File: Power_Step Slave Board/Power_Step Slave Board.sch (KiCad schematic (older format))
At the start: 13 parts

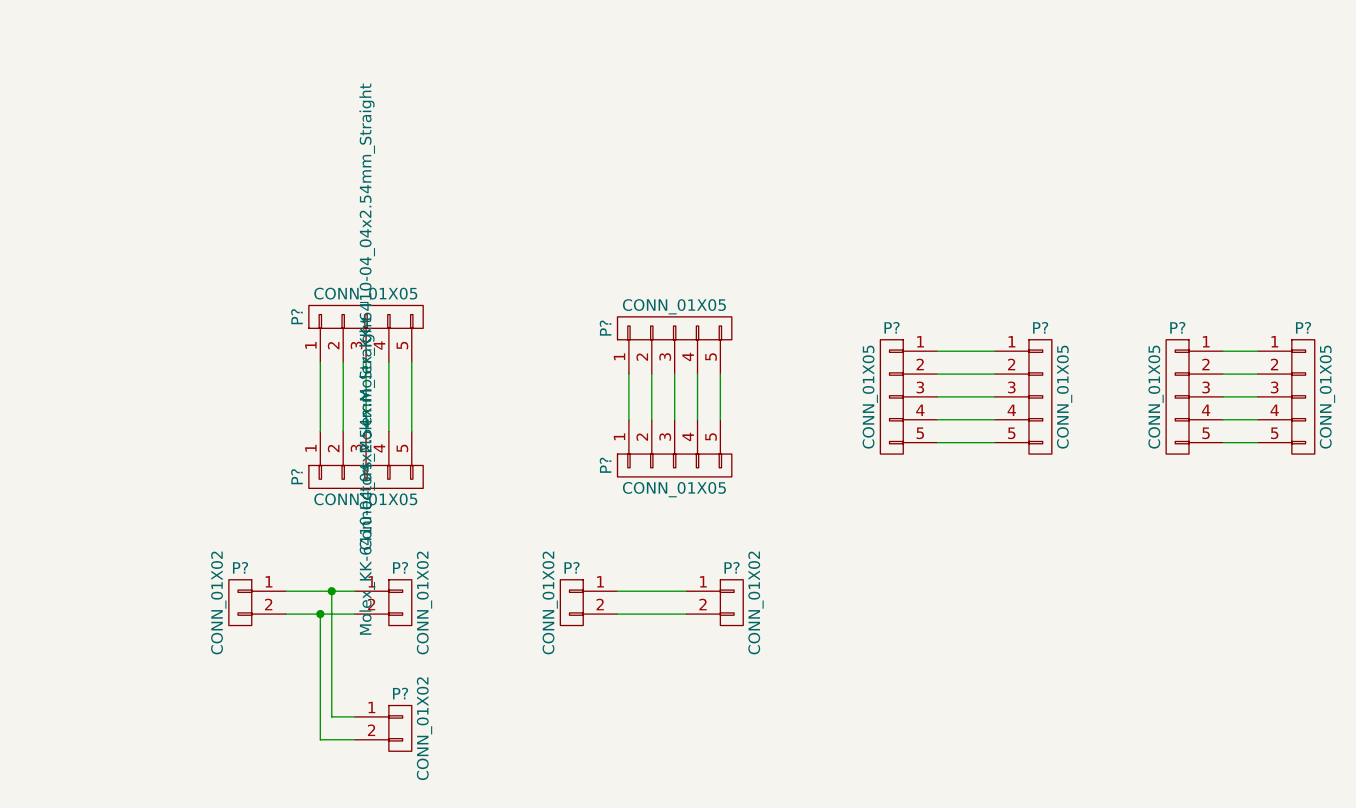
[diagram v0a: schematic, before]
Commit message: Updated connectors
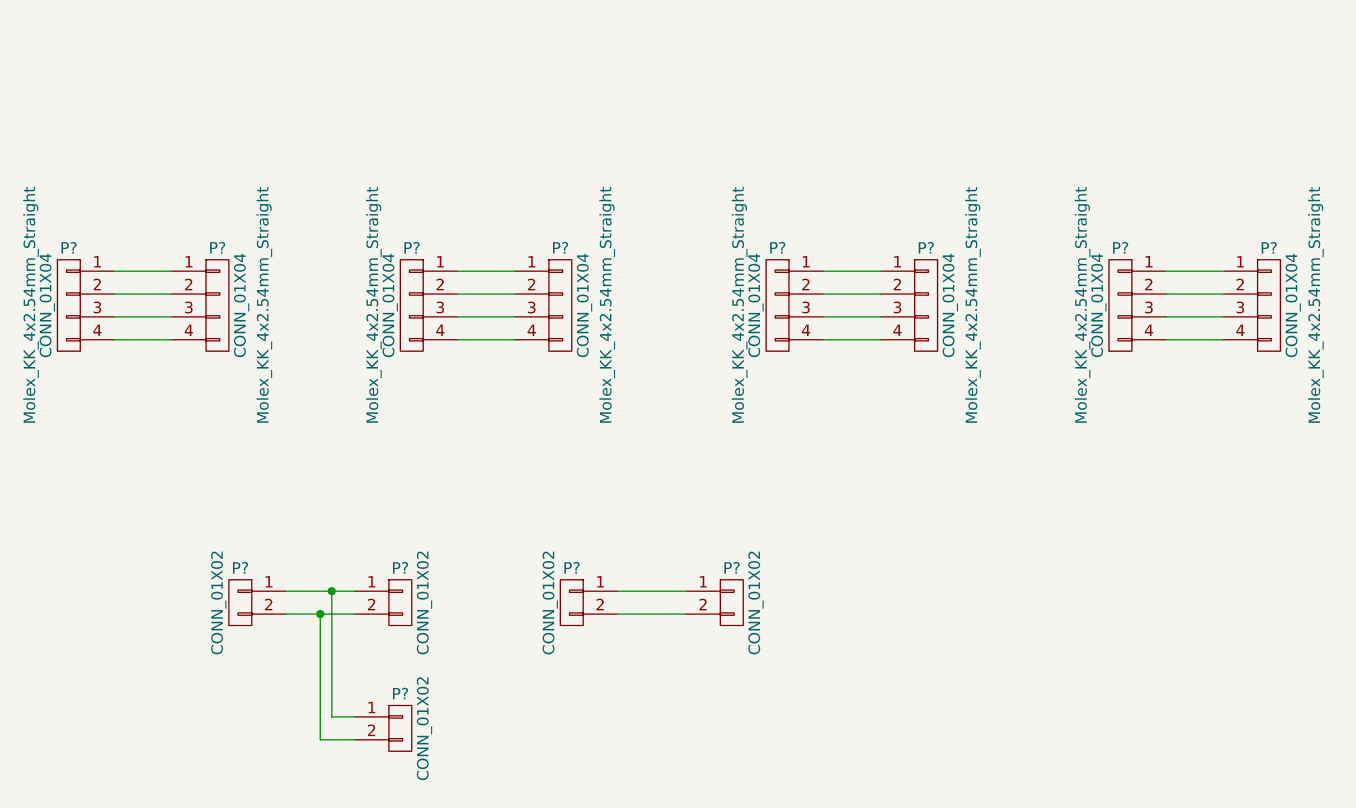
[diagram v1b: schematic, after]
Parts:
- removed P?: CONN_01X05, Molex_KK-6410-04_04x2.54mm_Straight, symbol CONN_01X05
- removed P?: CONN_01X05, Connectors_Molex:Molex_KK-6410-04_04x2.54mm_Straight, symbol CONN_01X05
- removed P? (x6): CONN_01X05, symbol CONN_01X05
- added P? (x8): CONN_01X04, Molex_KK_4x2.54mm_Straight, symbol CONN_01X04
- P?: footprint (none) -> ~
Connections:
- new net: P?.1 (P1), P?.1 (P1) (x4)
- new net: P?.2 (P2), P?.2 (P2) (x4)
- new net: P?.3 (P3), P?.3 (P3) (x4)
- new net: P?.4 (P4), P?.4 (P4) (x4)
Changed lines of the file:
@@
 $EndDescr
-$Comp
-L CONN_01X05 P?
-U 1 1 59DDF6DF
-P 2550 2200
-F 0 "P?" H 2550 2500 50  0000 C CNN
-F 1 "CONN_01X05" V 2650 2200 50  0000 C CNN
-F 2 "Molex_KK-6410-04_04x2.54mm_Straight" H 2550 2200 50  0000 C CNN
-F 3 "" H 2550 2200 50  0000 C CNN
-	1    2550 2200
-	0    -1   1    0
-$EndComp
-$Comp
-L CONN_01X05 P?
-U 1 1 59DDF732
-P 2550 1500
-F 0 "P?" H 2550 1800 50  0000 C CNN
-F 1 "CONN_01X05" V 2650 1500 50  0000 C CNN
-F 2 "Connectors_Molex:Molex_KK-6410-04_04x2.54mm_Straight" H 2550 1500 50  0000 C CNN
-F 3 "" H 2550 1500 50  0000 C CNN
-	1    2550 1500
-	0    -1   -1   0
-$EndComp
-$Comp
-L CONN_01X05 P?
-U 1 1 59DDF785
-P 3900 2150
-F 0 "P?" H 3900 2450 50  0000 C CNN
-F 1 "CONN_01X05" V 4000 2150 50  0000 C CNN
-F 2 "" H 3900 2150 50  0000 C CNN
-F 3 "" H 3900 2150 50  0000 C CNN
-	1    3900 2150
-	0    -1   1    0
-$EndComp
-$Comp
-L CONN_01X05 P?
-U 1 1 59DDF7DA
-P 3900 1550
-F 0 "P?" H 3900 1850 50  0000 C CNN
-F 1 "CONN_01X05" V 4000 1550 50  0000 C CNN
-F 2 "" H 3900 1550 50  0000 C CNN
-F 3 "" H 3900 1550 50  0000 C CNN
-	1    3900 1550
-	0    -1   -1   0
-$EndComp
-$Comp
-L CONN_01X05 P?
-U 1 1 59DDF859
-P 4850 1850
-F 0 "P?" H 4850 2150 50  0000 C CNN
-F 1 "CONN_01X05" V 4950 1850 50  0000 C CNN
-F 2 "" H 4850 1850 50  0000 C CNN
-F 3 "" H 4850 1850 50  0000 C CNN
-	1    4850 1850
-	-1   0    0    -1
-$EndComp
-$Comp
-L CONN_01X05 P?
-U 1 1 59DDF884
-P 5500 1850
-F 0 "P?" H 5500 2150 50  0000 C CNN
-F 1 "CONN_01X05" V 5600 1850 50  0000 C CNN
-F 2 "" H 5500 1850 50  0000 C CNN
-F 3 "" H 5500 1850 50  0000 C CNN
-	1    5500 1850
-	1    0    0    -1
-$EndComp
-$Comp
-L CONN_01X05 P?
-U 1 1 59DDF90B
-P 6100 1850
-F 0 "P?" H 6100 2150 50  0000 C CNN
-F 1 "CONN_01X05" V 6200 1850 50  0000 C CNN
-F 2 "" H 6100 1850 50  0000 C CNN
-F 3 "" H 6100 1850 50  0000 C CNN
-	1    6100 1850
-	-1   0    0    -1
-$EndComp
-$Comp
-L CONN_01X05 P?
-U 1 1 59DDF964
-P 6650 1850
-F 0 "P?" H 6650 2150 50  0000 C CNN
-F 1 "CONN_01X05" V 6750 1850 50  0000 C CNN
-F 2 "" H 6650 1850 50  0000 C CNN
-F 3 "" H 6650 1850 50  0000 C CNN
-	1    6650 1850
-	1    0    0    -1
-$EndComp
-Wire Wire Line
-	2350 2000 2350 1700
-Wire Wire Line
-	2450 1700 2450 2000
-Wire Wire Line
-	2550 2000 2550 1700
-Wire Wire Line
-	2650 1700 2650 2000
-Wire Wire Line
-	2750 2000 2750 1700
-Wire Wire Line
-	3700 1950 3700 1750
-Wire Wire Line
-	3800 1750 3800 1950
-Wire Wire Line
-	3900 1950 3900 1750
-Wire Wire Line
-	4000 1750 4000 1950
-Wire Wire Line
-	4100 1950 4100 1750
-Wire Wire Line
-	5050 2050 5300 2050
-Wire Wire Line
-	5300 1950 5050 1950
-Wire Wire Line
-	5050 1850 5300 1850
-Wire Wire Line
-	5300 1750 5050 1750
-Wire Wire Line
-	5050 1650 5300 1650
-Wire Wire Line
-	6300 1650 6450 1650
-Wire Wire Line
-	6450 1750 6300 1750
-Wire Wire Line
-	6300 1850 6450 1850
-Wire Wire Line
-	6450 1950 6300 1950
-Wire Wire Line
-	6300 2050 6450 2050
 $Comp
 L CONN_01X02 P?
@@
 F 0 "P?" H 2000 2900 50  0000 C CNN
 F 1 "CONN_01X02" V 2100 2750 50  0000 C CNN
-F 2 "" H 2000 2750 50  0000 C CNN
+F 2 "~" H 2000 2750 50  0000 C CNN
 F 3 "" H 2000 2750 50  0000 C CNN
 	1    2000 2750
@@
 Wire Wire Line
 	3950 2800 3650 2800
+$Comp
+L CONN_01X04 P?
+U 1 1 59E07C82
+P 1250 1450
+F 0 "P?" H 1250 1700 50  0000 C CNN
+F 1 "CONN_01X04" V 1350 1450 50  0000 C CNN
+F 2 "Molex_KK_4x2.54mm_Straight" V 1450 1450 50  0000 C BNN
+F 3 "" H 1250 1450 50  0000 C CNN
+	1    1250 1450
+	-1   0    0    -1
+$EndComp
+$Comp
+L CONN_01X04 P?
+U 1 1 59E07D10
+P 1900 1450
+F 0 "P?" H 1900 1700 50  0000 C CNN
+F 1 "CONN_01X04" V 2000 1450 50  0000 C CNN
+F 2 "Molex_KK_4x2.54mm_Straight" V 2100 1450 50  0000 C CNN
+F 3 "" H 1900 1450 50  0000 C CNN
+	1    1900 1450
+	1    0    0    -1
+$EndComp
+Wire Wire Line
+	1450 1300 1700 1300
+Wire Wire Line
+	1700 1400 1450 1400
+Wire Wire Line
+	1450 1500 1700 1500
+Wire Wire Line
+	1700 1600 1450 1600
+$Comp
+L CONN_01X04 P?
+U 1 1 59E081DD
+P 2750 1450
+F 0 "P?" H 2750 1700 50  0000 C CNN
+F 1 "CONN_01X04" V 2850 1450 50  0000 C CNN
+F 2 "Molex_KK_4x2.54mm_Straight" V 2950 1450 50  0000 C BNN
+F 3 "" H 2750 1450 50  0000 C CNN
+	1    2750 1450
+	-1   0    0    -1
+$EndComp
+$Comp
+L CONN_01X04 P?
+U 1 1 59E081E3
+P 3400 1450
+F 0 "P?" H 3400 1700 50  0000 C CNN
+F 1 "CONN_01X04" V 3500 1450 50  0000 C CNN
+F 2 "Molex_KK_4x2.54mm_Straight" V 3600 1450 50  0000 C CNN
+F 3 "" H 3400 1450 50  0000 C CNN
+	1    3400 1450
+	1    0    0    -1
+$EndComp
+Wire Wire Line
+	2950 1300 3200 1300
+Wire Wire Line
+	3200 1400 2950 1400
+Wire Wire Line
+	2950 1500 3200 1500
+Wire Wire Line
+	3200 1600 2950 1600
+$Comp
+L CONN_01X04 P?
+U 1 1 59E08812
+P 4350 1450
+F 0 "P?" H 4350 1700 50  0000 C CNN
+F 1 "CONN_01X04" V 4450 1450 50  0000 C CNN
+F 2 "Molex_KK_4x2.54mm_Straight" V 4550 1450 50  0000 C BNN
+F 3 "" H 4350 1450 50  0000 C CNN
+	1    4350 1450
+	-1   0    0    -1
+$EndComp
+$Comp
+L CONN_01X04 P?
+U 1 1 59E08818
+P 5000 1450
+F 0 "P?" H 5000 1700 50  0000 C CNN
+F 1 "CONN_01X04" V 5100 1450 50  0000 C CNN
+F 2 "Molex_KK_4x2.54mm_Straight" V 5200 1450 50  0000 C CNN
+F 3 "" H 5000 1450 50  0000 C CNN
+	1    5000 1450
+	1    0    0    -1
+$EndComp
+Wire Wire Line
+	4550 1300 4800 1300
+Wire Wire Line
+	4800 1400 4550 1400
+Wire Wire Line
+	4550 1500 4800 1500
+Wire Wire Line
+	4800 1600 4550 1600
+$Comp
+L CONN_01X04 P?
+U 1 1 59E08822
+P 5850 1450
+F 0 "P?" H 5850 1700 50  0000 C CNN
+F 1 "CONN_01X04" V 5950 1450 50  0000 C CNN
+F 2 "Molex_KK_4x2.54mm_Straight" V 6050 1450 50  0000 C BNN
+F 3 "" H 5850 1450 50  0000 C CNN
+	1    5850 1450
+	-1   0    0    -1
+$EndComp
+$Comp
+L CONN_01X04 P?
+U 1 1 59E08828
+P 6500 1450
+F 0 "P?" H 6500 1700 50  0000 C CNN
+F 1 "CONN_01X04" V 6600 1450 50  0000 C CNN
+F 2 "Molex_KK_4x2.54mm_Straight" V 6700 1450 50  0000 C CNN
+F 3 "" H 6500 1450 50  0000 C CNN
+	1    6500 1450
+	1    0    0    -1
+$EndComp
+Wire Wire Line
+	6050 1300 6300 1300
+Wire Wire Line
+	6300 1400 6050 1400
+Wire Wire Line
+	6050 1500 6300 1500
+Wire Wire Line
+	6300 1600 6050 1600
 $EndSCHEMATC

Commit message: added leds
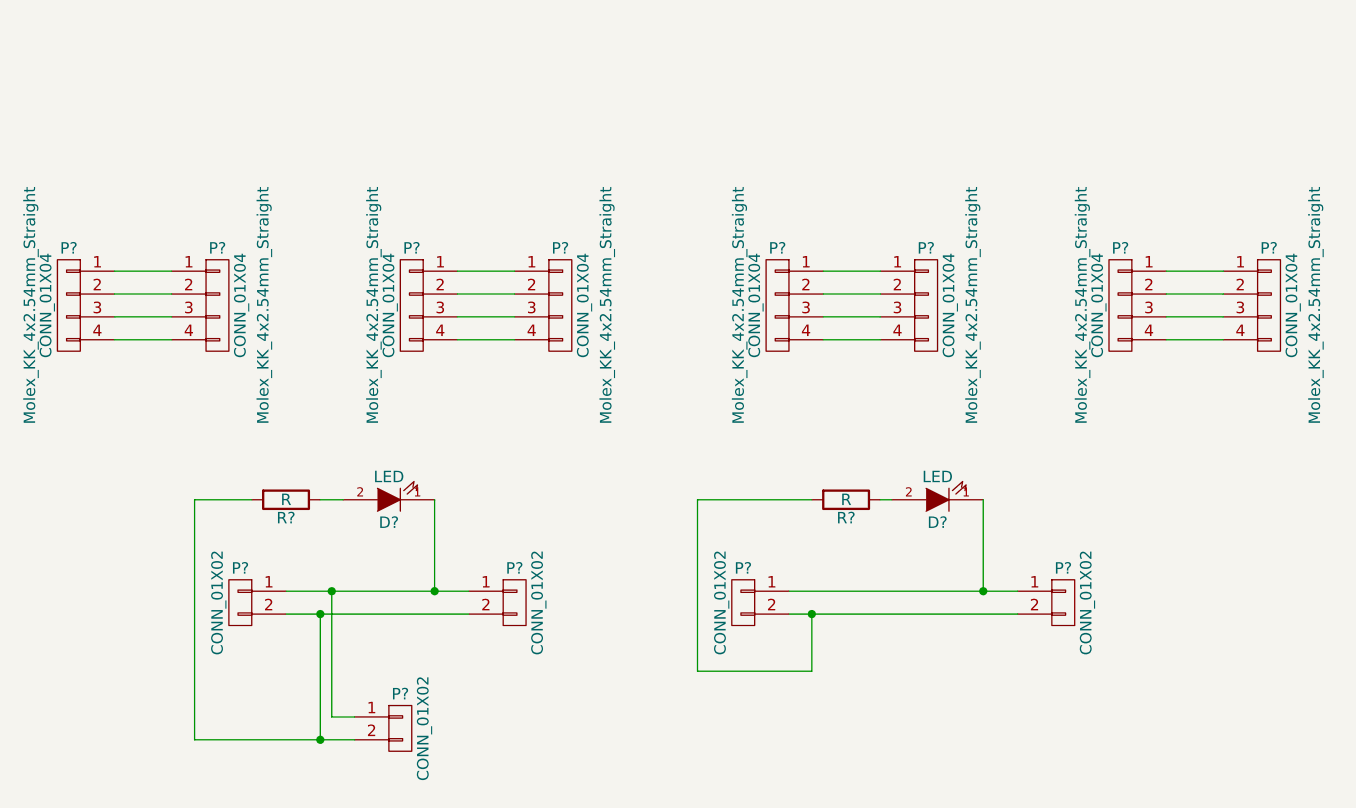
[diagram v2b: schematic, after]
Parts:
- added D? (x2): LED, symbol LED
- added R? (x2): R, symbol R
- P?: footprint ~ -> ASSETS:CONN_ON_SHORE_2x_15A
- P? (x4): footprint (none) -> ASSETS:CONN_ON_SHORE_2x_15A
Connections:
- net at P?.1 (P1), P?.1 (P1), P?.1 (P1): now also D?.1 (K)
- net at P?.2 (P2), P?.2 (P2), P?.2 (P2): now also R?.2
- net at P?.1 (P1), P?.1 (P1): now also D?.1 (K)
- net at P?.2 (P2), P?.2 (P2): now also R?.2
- new net: D?.2 (A), R?.1 (x2)
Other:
- moved on the sheet: P?
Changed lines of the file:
@@
 F 0 "P?" H 2000 2900 50  0000 C CNN
 F 1 "CONN_01X02" V 2100 2750 50  0000 C CNN
-F 2 "~" H 2000 2750 50  0000 C CNN
+F 2 "ASSETS:CONN_ON_SHORE_2x_15A" H 2000 2750 50  0001 C CNN
 F 3 "" H 2000 2750 50  0000 C CNN
 	1    2000 2750
@@
 L CONN_01X02 P?
 U 1 1 59DE1351
-P 2700 2750
-F 0 "P?" H 2700 2900 50  0000 C CNN
-F 1 "CONN_01X02" V 2800 2750 50  0000 C CNN
-F 2 "" H 2700 2750 50  0000 C CNN
-F 3 "" H 2700 2750 50  0000 C CNN
-	1    2700 2750
+P 3200 2750
+F 0 "P?" H 3200 2900 50  0000 C CNN
+F 1 "CONN_01X02" V 3300 2750 50  0000 C CNN
+F 2 "ASSETS:CONN_ON_SHORE_2x_15A" H 3200 2750 50  0001 C BNN
+F 3 "" H 3200 2750 50  0000 C CNN
+	1    3200 2750
 	1    0    0    -1
 $EndComp
@@
 F 0 "P?" H 2700 3450 50  0000 C CNN
 F 1 "CONN_01X02" V 2800 3300 50  0000 C CNN
-F 2 "" H 2700 3300 50  0000 C CNN
+F 2 "ASSETS:CONN_ON_SHORE_2x_15A" H 2700 3300 50  0001 C CNN
 F 3 "" H 2700 3300 50  0000 C CNN
 	1    2700 3300
@@
 L CONN_01X02 P?
 U 1 1 59DE1578
-P 3450 2750
-F 0 "P?" H 3450 2900 50  0000 C CNN
-F 1 "CONN_01X02" V 3550 2750 50  0000 C CNN
-F 2 "" H 3450 2750 50  0000 C CNN
-F 3 "" H 3450 2750 50  0000 C CNN
-	1    3450 2750
+P 4200 2750
+F 0 "P?" H 4200 2900 50  0000 C CNN
+F 1 "CONN_01X02" V 4300 2750 50  0000 C CNN
+F 2 "ASSETS:CONN_ON_SHORE_2x_15A" H 4200 2750 50  0001 C CNN
+F 3 "" H 4200 2750 50  0000 C CNN
+	1    4200 2750
 	-1   0    0    -1
 $EndComp
@@
 L CONN_01X02 P?
 U 1 1 59DE15C8
-P 4150 2750
-F 0 "P?" H 4150 2900 50  0000 C CNN
-F 1 "CONN_01X02" V 4250 2750 50  0000 C CNN
-F 2 "" H 4150 2750 50  0000 C CNN
-F 3 "" H 4150 2750 50  0000 C CNN
-	1    4150 2750
-	1    0    0    -1
-$EndComp
-Wire Wire Line
-	2200 2800 2500 2800
-Wire Wire Line
-	2350 2800 2350 3350
-Wire Wire Line
-	2350 3350 2500 3350
-Connection ~ 2350 2800
-Wire Wire Line
-	2200 2700 2500 2700
-Wire Wire Line
-	2400 2700 2400 3250
-Wire Wire Line
-	2400 3250 2500 3250
-Connection ~ 2400 2700
-Wire Wire Line
-	3650 2700 3950 2700
-Wire Wire Line
-	3950 2800 3650 2800
+P 5600 2750
+F 0 "P?" H 5600 2900 50  0000 C CNN
+F 1 "CONN_01X02" V 5700 2750 50  0000 C CNN
+F 2 "ASSETS:CONN_ON_SHORE_2x_15A" H 5600 2750 50  0001 C CNN
+F 3 "" H 5600 2750 50  0000 C CNN
+	1    5600 2750
+	1    0    0    -1
+$EndComp
 $Comp
 L CONN_01X04 P?
@@
 	1    0    0    -1
 $EndComp
-Wire Wire Line
-	1450 1300 1700 1300
-Wire Wire Line
-	1700 1400 1450 1400
-Wire Wire Line
-	1450 1500 1700 1500
-Wire Wire Line
-	1700 1600 1450 1600
 $Comp
 L CONN_01X04 P?
@@
 	1    0    0    -1
 $EndComp
-Wire Wire Line
-	2950 1300 3200 1300
-Wire Wire Line
-	3200 1400 2950 1400
-Wire Wire Line
-	2950 1500 3200 1500
-Wire Wire Line
-	3200 1600 2950 1600
 $Comp
 L CONN_01X04 P?
@@
 	1    0    0    -1
 $EndComp
-Wire Wire Line
-	4550 1300 4800 1300
-Wire Wire Line
-	4800 1400 4550 1400
-Wire Wire Line
-	4550 1500 4800 1500
-Wire Wire Line
-	4800 1600 4550 1600
 $Comp
 L CONN_01X04 P?
@@
 	1    0    0    -1
 $EndComp
+$Comp
+L R R?
+U 1 1 59E0902D
+P 2200 2300
+F 0 "R?" V 2280 2300 50  0000 C CNN
+F 1 "R" V 2200 2300 50  0000 C CNN
+F 2 "" V 2130 2300 50  0000 C CNN
+F 3 "" H 2200 2300 50  0000 C CNN
+	1    2200 2300
+	0    1    1    0
+$EndComp
+$Comp
+L LED D?
+U 1 1 59E0909A
+P 2650 2300
+F 0 "D?" H 2650 2400 50  0000 C CNN
+F 1 "LED" H 2650 2200 50  0000 C CNN
+F 2 "" H 2650 2300 50  0000 C CNN
+F 3 "" H 2650 2300 50  0000 C CNN
+	1    2650 2300
+	-1   0    0    1
+$EndComp
+$Comp
+L R R?
+U 1 1 59E098E0
+P 4650 2300
+F 0 "R?" V 4730 2300 50  0000 C CNN
+F 1 "R" V 4650 2300 50  0000 C CNN
+F 2 "" V 4580 2300 50  0000 C CNN
+F 3 "" H 4650 2300 50  0000 C CNN
+	1    4650 2300
+	0    1    1    0
+$EndComp
+$Comp
+L LED D?
+U 1 1 59E098E6
+P 5050 2300
+F 0 "D?" H 5050 2400 50  0000 C CNN
+F 1 "LED" H 5050 2200 50  0000 C CNN
+F 2 "" H 5050 2300 50  0000 C CNN
+F 3 "" H 5050 2300 50  0000 C CNN
+	1    5050 2300
+	-1   0    0    1
+$EndComp
+Wire Wire Line
+	2200 2800 3000 2800
+Wire Wire Line
+	2350 2800 2350 3350
+Wire Wire Line
+	1800 3350 2500 3350
+Connection ~ 2350 2800
+Wire Wire Line
+	2200 2700 3000 2700
+Wire Wire Line
+	2400 2700 2400 3250
+Wire Wire Line
+	2400 3250 2500 3250
+Connection ~ 2400 2700
+Wire Wire Line
+	4400 2700 5400 2700
+Wire Wire Line
+	5400 2800 4400 2800
+Wire Wire Line
+	1450 1300 1700 1300
+Wire Wire Line
+	1700 1400 1450 1400
+Wire Wire Line
+	1450 1500 1700 1500
+Wire Wire Line
+	1700 1600 1450 1600
+Wire Wire Line
+	2950 1300 3200 1300
+Wire Wire Line
+	3200 1400 2950 1400
+Wire Wire Line
+	2950 1500 3200 1500
+Wire Wire Line
+	3200 1600 2950 1600
+Wire Wire Line
+	4550 1300 4800 1300
+Wire Wire Line
+	4800 1400 4550 1400
+Wire Wire Line
+	4550 1500 4800 1500
+Wire Wire Line
+	4800 1600 4550 1600
 Wire Wire Line
 	6050 1300 6300 1300
@@
 Wire Wire Line
 	6300 1600 6050 1600
+Wire Wire Line
+	2350 2300 2450 2300
+Wire Wire Line
+	2850 2300 2850 2700
+Connection ~ 2850 2700
+Wire Wire Line
+	2050 2300 1800 2300
+Wire Wire Line
+	1800 2300 1800 3350
+Connection ~ 2350 3350
+Wire Wire Line
+	4800 2300 4850 2300
+Wire Wire Line
+	4000 2300 4500 2300
+Wire Wire Line
+	4000 2300 4000 3050
+Wire Wire Line
+	4000 3050 4500 3050
+Wire Wire Line
+	4500 3050 4500 2800
+Connection ~ 4500 2800
+Wire Wire Line
+	5250 2300 5250 2700
+Connection ~ 5250 2700
 $EndSCHEMATC
